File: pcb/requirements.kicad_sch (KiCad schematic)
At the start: 10 parts

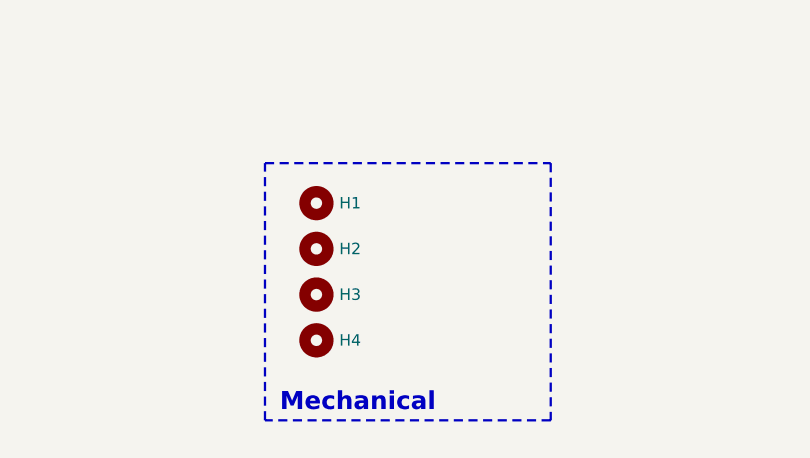
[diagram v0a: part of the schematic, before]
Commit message: Updates for consistency
Changed mounting holes to grounded
Updated power connectors
Added power ESD protection
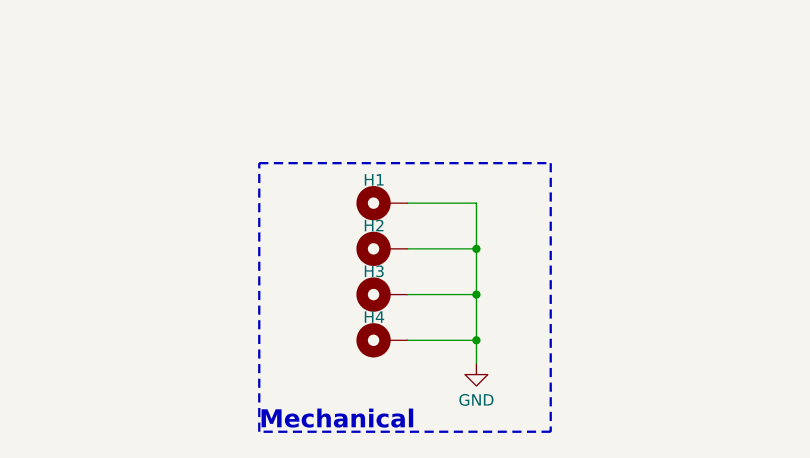
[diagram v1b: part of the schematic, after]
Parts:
- H1, H2, H3, H4: symbol Mechanical:MountingHole -> CRGM Mechanical:MountingHole_Pad
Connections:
- new net GND: H1.1, H2.1, H3.1, H4.1

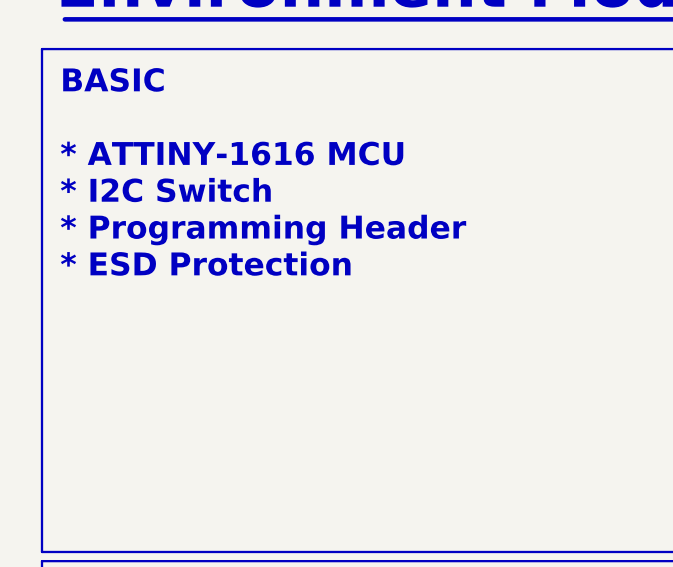
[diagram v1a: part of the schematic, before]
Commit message: Swapped temp sensor for more popular model
Changed HDC1080 for AHT20
Updated reference layer
Updated renders
Updated requirements
Fixed models
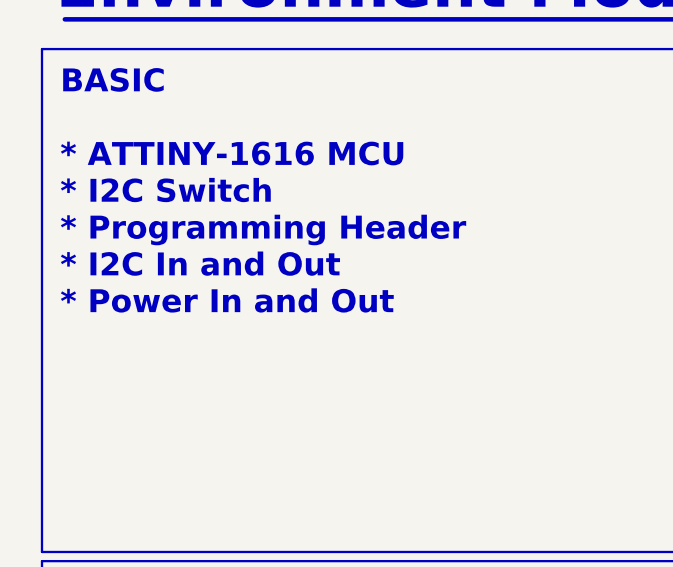
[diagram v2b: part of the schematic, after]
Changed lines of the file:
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@@
 		)
 	)
-	(text_box "BASIC\n\n* ATTINY-1616 MCU\n* I2C Switch\n* Programming Header\n* ESD Protection\n\n"
+	(text_box "BASIC\n\n* ATTINY-1616 MCU\n* I2C Switch\n* Programming Header\n* I2C In and Out\n* Power In and Out\n\n"
 		(exclude_from_sim yes)
 		(at 17.78 25.4 0)
